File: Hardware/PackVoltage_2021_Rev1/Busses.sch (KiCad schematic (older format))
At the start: 0 parts

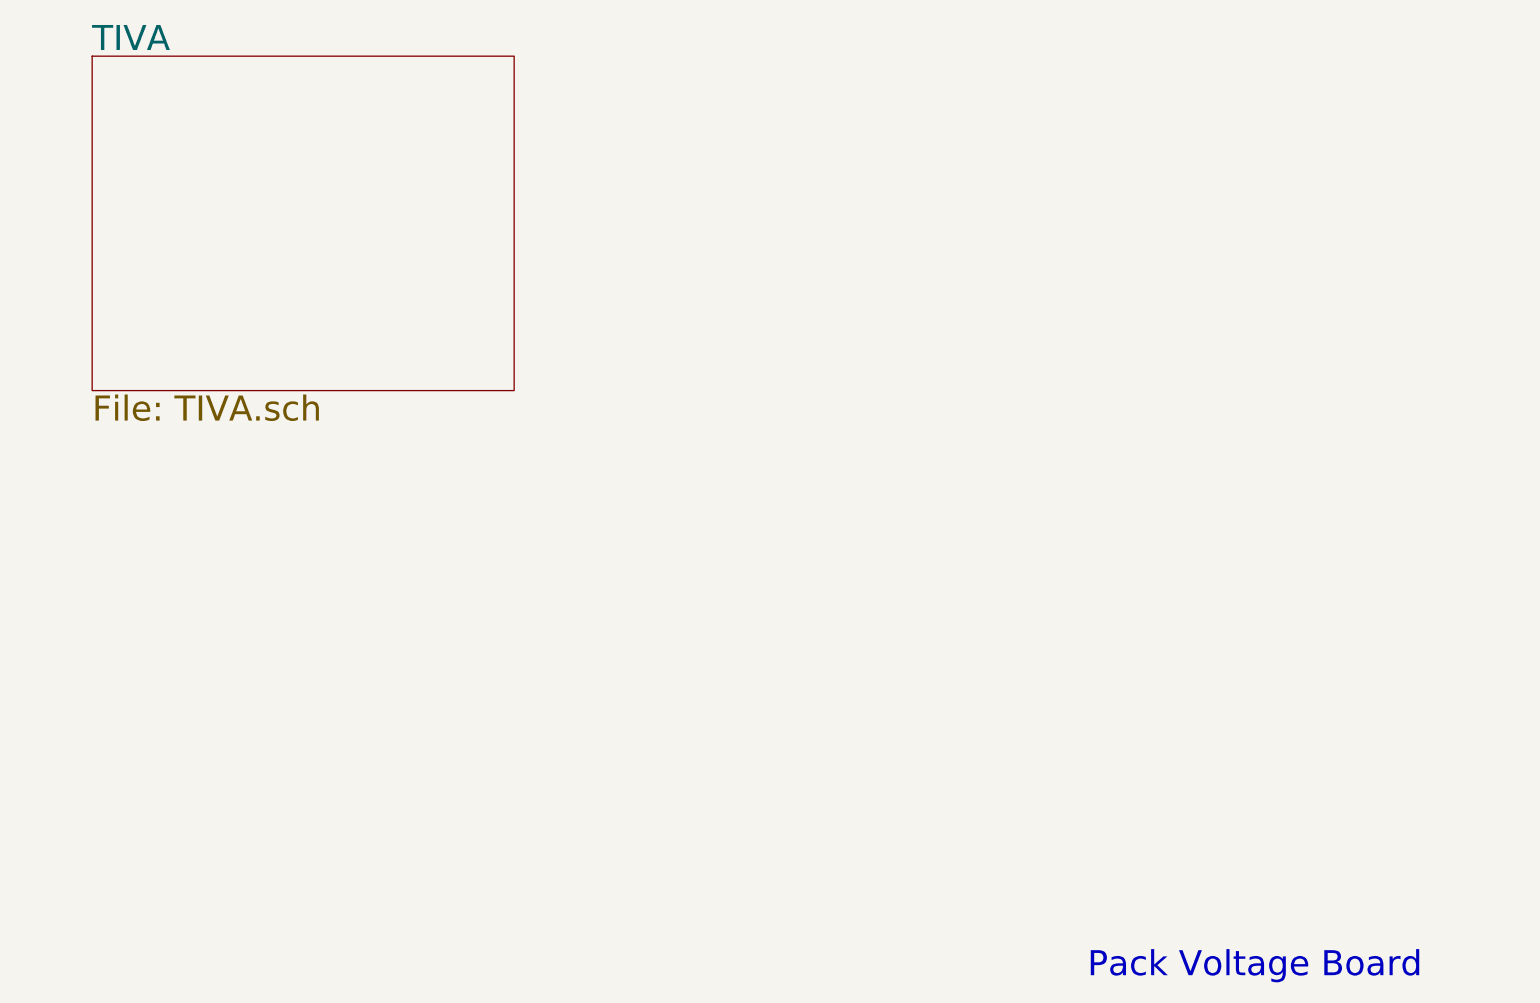
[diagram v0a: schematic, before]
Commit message: Busses & Library Files
Started stuff for adding new libraries, made sheet for busses, but don't have any components
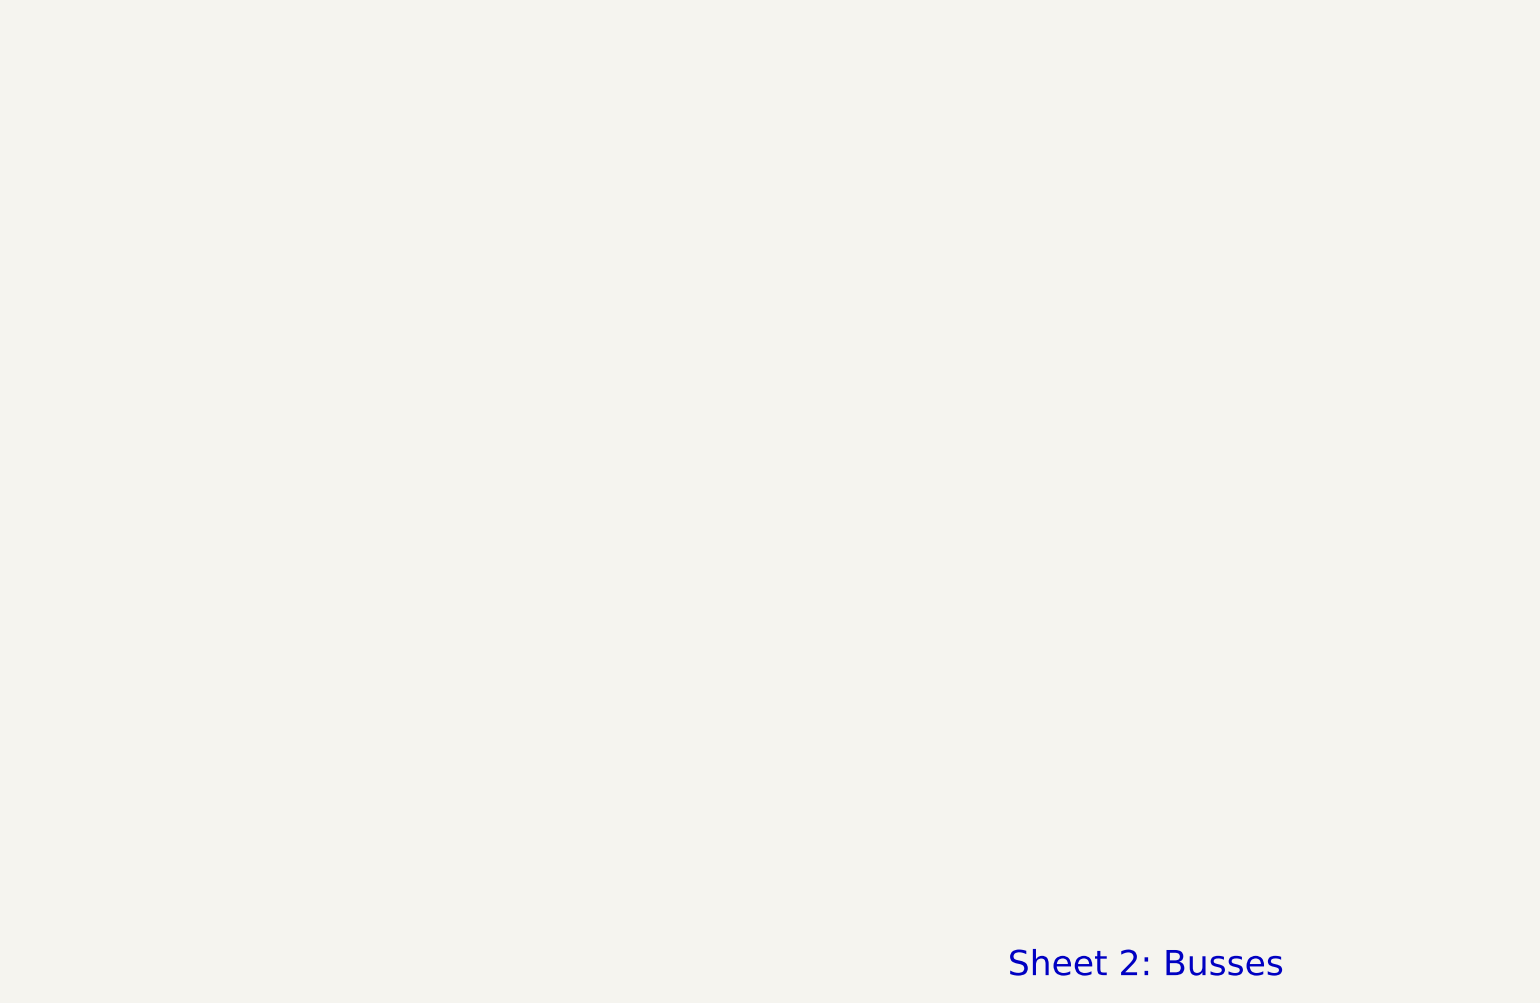
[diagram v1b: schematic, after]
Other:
- note added: "Sheet 2: Busses"
- note removed: "Pack Voltage Board"
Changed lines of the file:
@@
 $Descr A4 11693 8268
 encoding utf-8
-Sheet 1 2
+Sheet 3 3
 Title ""
 Date ""
@@
 Comment4 ""
 $EndDescr
-Text Notes 7700 6950 0    157  ~ 0
-Pack Voltage Board
-$Sheet
-S 1450 1150 2650 2100
-U 5F74F238
-F0 "TIVA" 157
-F1 "TIVA.sch" 157
-$EndSheet
+Text Notes 7200 6950 0    158  ~ 0
+Sheet 2: Busses
 $EndSCHEMATC

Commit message: Started Current and LT1910 circuits
Mosfet and current sensor for one port made
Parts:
- added F?: Fuse, symbol Device:Fuse
- added Q?: Q_NMOS_DGS, symbol Device:Q_NMOS_DGS
- added R?: R, symbol Device:R
- added U?: LT1910, symbol MRDT_ICs:LT1910
- added U?: INA195, Package_TO_SOT_SMD:SOT-23-5, symbol Amplifier_Current:INA195
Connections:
- net labels added: +5V, Current_Sensor_M1, GND
- wire segments 0 -> 11
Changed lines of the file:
@@
 Text Notes 7200 6950 0    158  ~ 0
 Sheet 2: Busses
+$Comp
+L Device:Q_NMOS_DGS Q?
+U 1 1 5F768EE8
+P 3300 1550
+F 0 "Q?" V 3549 1550 50  0000 C CNN
+F 1 "Q_NMOS_DGS" V 3640 1550 50  0000 C CNN
+F 2 "" H 3500 1650 50  0001 C CNN
+F 3 "~" H 3300 1550 50  0001 C CNN
+	1    3300 1550
+	0    1    1    0
+$EndComp
+$Comp
+L MRDT_ICs:LT1910 U?
+U 1 1 5F76B064
+P 1600 1900
+F 0 "U?" H 1975 2587 60  0000 C CNN
+F 1 "LT1910" H 1975 2481 60  0000 C CNN
+F 2 "" H 1600 1900 60  0001 C CNN
+F 3 "" H 1600 1900 60  0001 C CNN
+	1    1600 1900
+	1    0    0    -1
+$EndComp
+$Comp
+L Amplifier_Current:INA195 U?
+U 1 1 5F76DF77
+P 4350 1750
+F 0 "U?" H 4694 1796 50  0000 L CNN
+F 1 "INA195" H 4694 1705 50  0000 L CNN
+F 2 "Package_TO_SOT_SMD:SOT-23-5" H 4350 1750 50  0001 C CNN
+F 3 "http://www.ti.com/lit/ds/symlink/ina193.pdf" H 4350 1750 50  0001 C CNN
+	1    4350 1750
+	1    0    0    -1
+$EndComp
+$Comp
+L power:+5V #PWR?
+U 1 1 5F771D8F
+P 4250 1250
+F 0 "#PWR?" H 4250 1100 50  0001 C CNN
+F 1 "+5V" H 4265 1423 50  0000 C CNN
+F 2 "" H 4250 1250 50  0001 C CNN
+F 3 "" H 4250 1250 50  0001 C CNN
+	1    4250 1250
+	1    0    0    -1
+$EndComp
+Wire Wire Line
+	4250 1250 4250 1450
+$Comp
+L power:GND #PWR?
+U 1 1 5F77250D
+P 4250 2200
+F 0 "#PWR?" H 4250 1950 50  0001 C CNN
+F 1 "GND" H 4255 2027 50  0000 C CNN
+F 2 "" H 4250 2200 50  0001 C CNN
+F 3 "" H 4250 2200 50  0001 C CNN
+	1    4250 2200
+	1    0    0    -1
+$EndComp
+Wire Wire Line
+	4250 2050 4250 2200
+Text GLabel 5050 1750 2    50   Output ~ 0
+Current_Sensor_M1
+Wire Wire Line
+	4650 1750 5050 1750
+Wire Wire Line
+	3500 1650 4050 1650
+$Comp
+L power:GND #PWR?
+U 1 1 5F77CED8
+P 2000 2250
+F 0 "#PWR?" H 2000 2000 50  0001 C CNN
+F 1 "GND" H 2005 2077 50  0000 C CNN
+F 2 "" H 2000 2250 50  0001 C CNN
+F 3 "" H 2000 2250 50  0001 C CNN
+	1    2000 2250
+	1    0    0    -1
+$EndComp
+Wire Wire Line
+	2000 2100 2000 2200
+Wire Wire Line
+	2950 1800 2950 1350
+Wire Wire Line
+	2950 1350 3300 1350
+$Comp
+L Device:Fuse F?
+U 1 1 5F78099C
+P 2550 1150
+F 0 "F?" H 2610 1196 50  0000 L CNN
+F 1 "Fuse" H 2610 1105 50  0000 L CNN
+F 2 "" V 2480 1150 50  0001 C CNN
+F 3 "~" H 2550 1150 50  0001 C CNN
+	1    2550 1150
+	1    0    0    -1
+$EndComp
+$Comp
+L Device:R R?
+U 1 1 5F78141C
+P 1100 1500
+F 0 "R?" V 893 1500 50  0000 C CNN
+F 1 "R" V 984 1500 50  0000 C CNN
+F 2 "" V 1030 1500 50  0001 C CNN
+F 3 "~" H 1100 1500 50  0001 C CNN
+	1    1100 1500
+	0    1    1    0
+$EndComp
+Wire Wire Line
+	2550 1800 2950 1800
+Wire Wire Line
+	2000 2200 2750 2200
+Wire Wire Line
+	2750 2200 2750 2100
+Connection ~ 2000 2200
+Wire Wire Line
+	2000 2200 2000 2250
 $EndSCHEMATC
